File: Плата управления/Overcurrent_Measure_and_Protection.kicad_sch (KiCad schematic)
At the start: 15 parts, among them U5 LMV7239M5, U7 AD8210, U8 LMV324

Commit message: Поенял усилитель измерительный AD8210 на automotive исполнение INA283AID
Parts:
- removed R29: 1k, Resistor_SMD:R_0603_1608Metric_Pad0.98x0.95mm_HandSolder, symbol Device:R_Small
- removed R29: 1.6k, Resistor_SMD:R_0603_1608Metric_Pad0.98x0.95mm_HandSolder, symbol Device:R_Small
- removed U7: AD8210, Package_SO:SOIC-8_3.9x4.9mm_P1.27mm, symbol Amplifier_Current:AD8210
- removed U8: LMV324, Package_SO:SOIC-14_3.9x8.7mm_P1.27mm, symbol Amplifier_Operational:LMV324
- added U4: INA283, symbol Amplifier_Current:INA283
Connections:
- net +3.3V: now also C17.1, R29.1, U4.3 (REF2), U4.6 (V+)
- net DC_Current_MCU: now also R29.2
- net GND: now also C17.2, U4.2 (GND), U4.7 (REF1); no longer C17.1
- net Shunt_1: now also U4.8 (+)
- net Shunt_2: now also U4.1 (-)
- net at R30.1: now also U4.5
- removed net +5V: C17.2, R29.1

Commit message: Заменил датчик положения ротора на NSM3012
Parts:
- U4: footprint (none) -> Package_SO:SOIC-8_3.9x4.9mm_P1.27mm
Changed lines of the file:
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@@
       (effects (font (size 1.27 1.27)))
     )
-    (property "Footprint" "" (at 148.59 138.43 0)
+    (property "Footprint" "Package_SO:SOIC-8_3.9x4.9mm_P1.27mm" (at 148.59 138.43 0)
       (effects (font (size 1.27 1.27)) hide)
     )

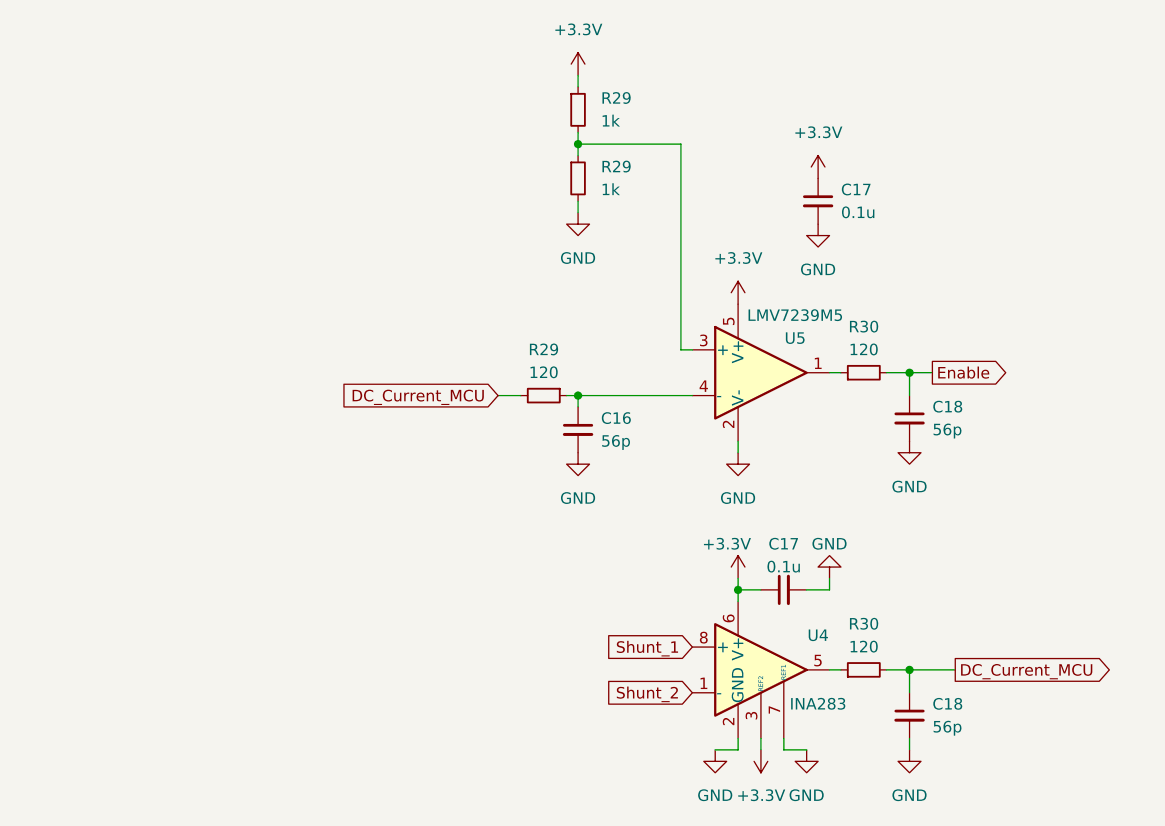
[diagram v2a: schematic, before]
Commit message: Добавил питание MCU и кварц на 8Мгц
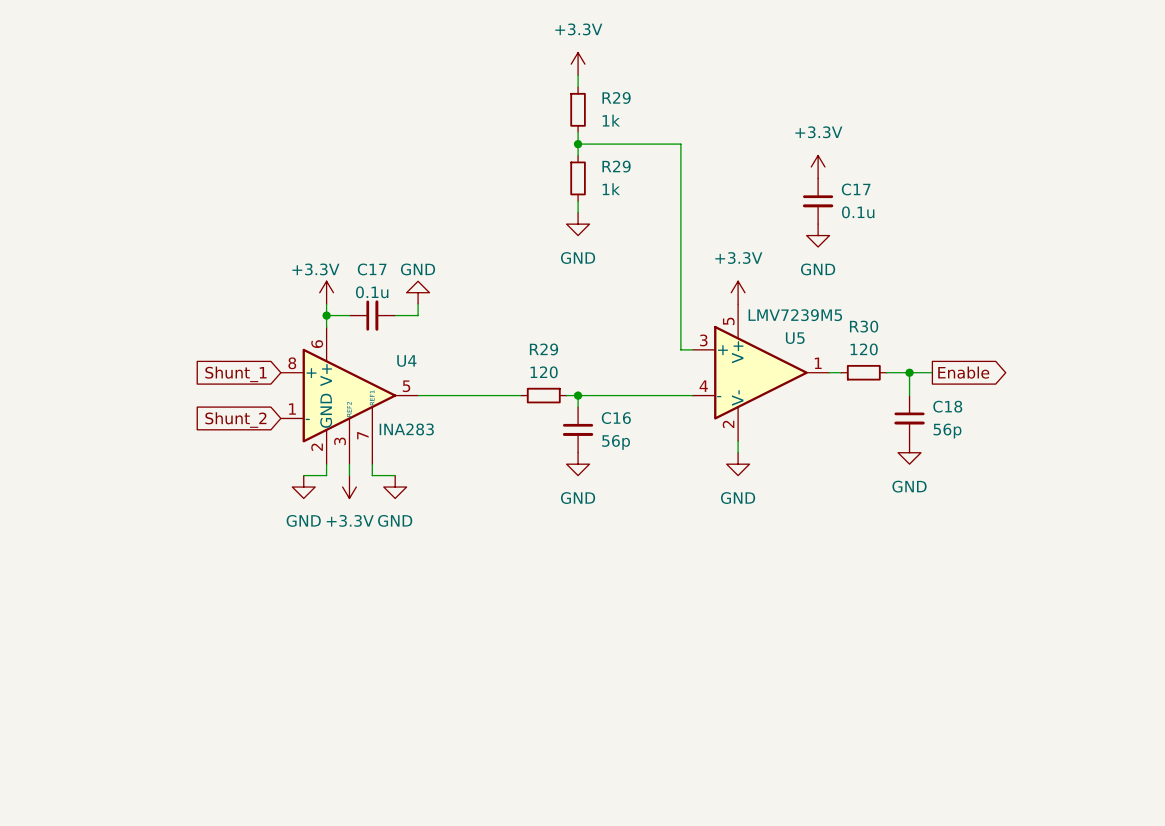
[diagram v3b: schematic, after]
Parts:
- removed C18: 56p, Capacitor_SMD:C_0603_1608Metric_Pad1.08x0.95mm_HandSolder, symbol Device:C_Small
- removed R30: 120, Resistor_SMD:R_0603_1608Metric_Pad0.98x0.95mm_HandSolder, symbol Device:R_Small
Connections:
- net DC_Current_MCU is gone; now on an unnamed net: R29.2
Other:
- moved on the sheet: C17, U4
